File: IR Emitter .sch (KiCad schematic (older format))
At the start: 19 parts

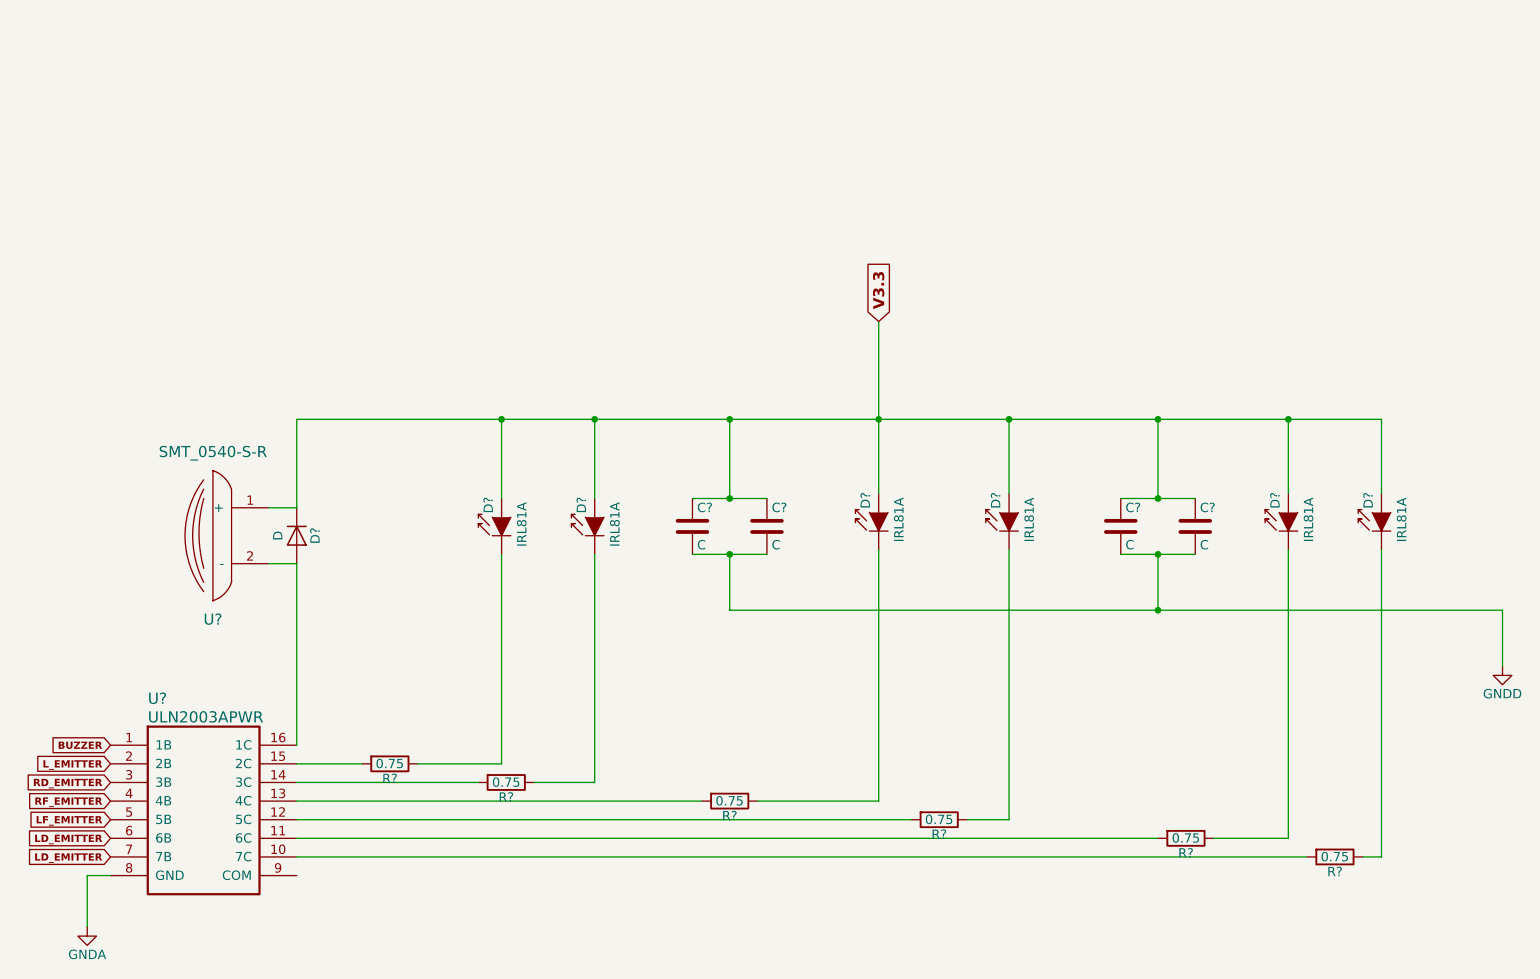
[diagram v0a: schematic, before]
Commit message: created footprint for linear requlator
added footprint for microcontroller linear requlator
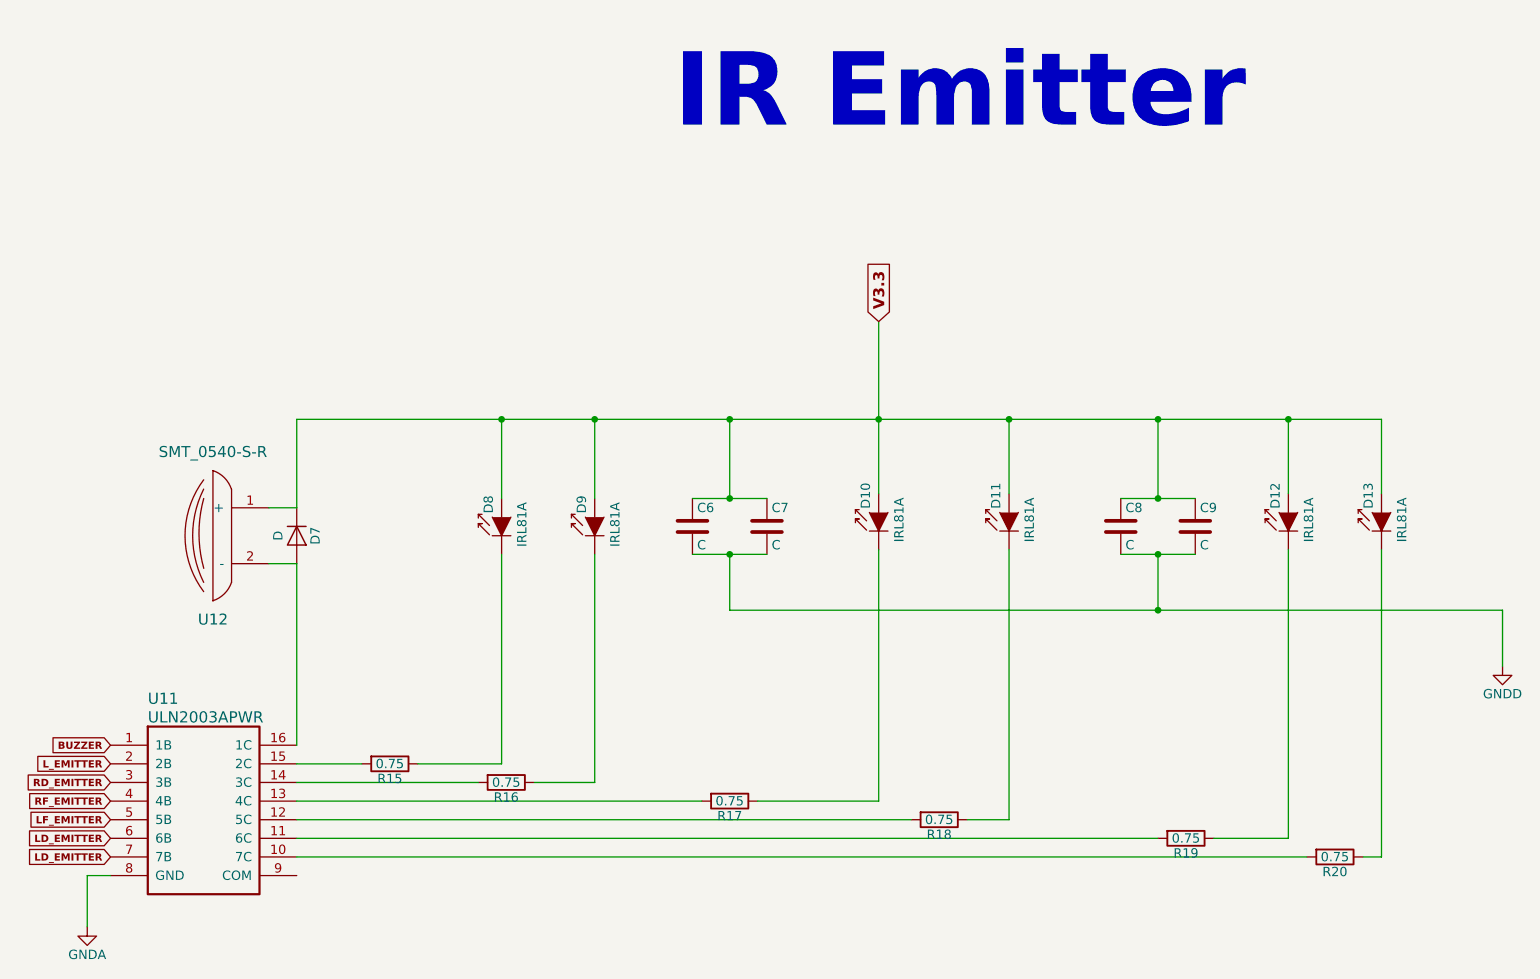
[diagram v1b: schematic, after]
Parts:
- C6, C7, C8, C9: renamed from C?; footprint (none) -> Capacitors_SMD:C_0603
- D10, D11, D12, D13, D8, D9: renamed from D?; footprint LEDs:LED_SideEmitter_Rectangular_W4.5mm_H1.6mm -> LEDs:LED_D5.0mm_Horizontal_O3.81mm_Z3.0mm
- D7: renamed from D?; footprint (none) -> Diodes_SMD:D_0603
- R15, R16, R17, R18, R19, R20: renamed from R?; footprint (none) -> Resistors_SMD:R_0603
- U11: renamed from U?; footprint (none) -> sop:TSSOP16
- U12: renamed from U?; footprint (none) -> micromouse:Buzzer_SMT-0540-S-R
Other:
- note added: "IR Emitter"
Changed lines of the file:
@@
 $EndDescr
 $Comp
-L IRL81A D?
+L IRL81A D9
 U 1 1 59460522
 P 3475 3450
-F 0 "D?" H 3495 3520 50  0000 L CNN
+F 0 "D9" H 3495 3520 50  0000 L CNN
 F 1 "IRL81A" H 3435 3340 50  0000 C CNN
-F 2 "LEDs:LED_SideEmitter_Rectangular_W4.5mm_H1.6mm" H 3475 3625 50  0001 C CNN
+F 2 "LEDs:LED_D5.0mm_Horizontal_O3.81mm_Z3.0mm" H 3475 3625 50  0001 C CNN
 F 3 "" H 3425 3450 50  0000 C CNN
 	1    3475 3450
@@
 $EndComp
 $Comp
-L IRL81A D?
+L IRL81A D10
 U 1 1 59460598
 P 5000 3425
-F 0 "D?" H 5020 3495 50  0000 L CNN
+F 0 "D10" H 5020 3495 50  0000 L CNN
 F 1 "IRL81A" H 4960 3315 50  0000 C CNN
-F 2 "LEDs:LED_SideEmitter_Rectangular_W4.5mm_H1.6mm" H 5000 3600 50  0001 C CNN
+F 2 "LEDs:LED_D5.0mm_Horizontal_O3.81mm_Z3.0mm" H 5000 3600 50  0001 C CNN
 F 3 "" H 4950 3425 50  0000 C CNN
 	1    5000 3425
@@
 $EndComp
 $Comp
-L IRL81A D?
+L IRL81A D11
 U 1 1 5946062F
 P 5700 3425
-F 0 "D?" H 5720 3495 50  0000 L CNN
+F 0 "D11" H 5720 3495 50  0000 L CNN
 F 1 "IRL81A" H 5660 3315 50  0000 C CNN
-F 2 "LEDs:LED_SideEmitter_Rectangular_W4.5mm_H1.6mm" H 5700 3600 50  0001 C CNN
+F 2 "LEDs:LED_D5.0mm_Horizontal_O3.81mm_Z3.0mm" H 5700 3600 50  0001 C CNN
 F 3 "" H 5650 3425 50  0000 C CNN
 	1    5700 3425
@@
 $EndComp
 $Comp
-L IRL81A D?
+L IRL81A D12
 U 1 1 59460667
 P 7200 3425
-F 0 "D?" H 7220 3495 50  0000 L CNN
+F 0 "D12" H 7220 3495 50  0000 L CNN
 F 1 "IRL81A" H 7160 3315 50  0000 C CNN
-F 2 "LEDs:LED_SideEmitter_Rectangular_W4.5mm_H1.6mm" H 7200 3600 50  0001 C CNN
+F 2 "LEDs:LED_D5.0mm_Horizontal_O3.81mm_Z3.0mm" H 7200 3600 50  0001 C CNN
 F 3 "" H 7150 3425 50  0000 C CNN
 	1    7200 3425
@@
 $EndComp
 $Comp
-L R R?
+L R R15
 U 1 1 594607AD
 P 2375 4775
-F 0 "R?" V 2455 4775 50  0000 C CNN
+F 0 "R15" V 2455 4775 50  0000 C CNN
 F 1 "0.75" V 2375 4775 50  0000 C CNN
-F 2 "" V 2305 4775 50  0001 C CNN
+F 2 "Resistors_SMD:R_0603" V 2305 4775 50  0001 C CNN
 F 3 "" H 2375 4775 50  0001 C CNN
 	1    2375 4775
@@
 $EndComp
 $Comp
-L R R?
+L R R16
 U 1 1 59460927
 P 3000 4875
-F 0 "R?" V 3080 4875 50  0000 C CNN
+F 0 "R16" V 3080 4875 50  0000 C CNN
 F 1 "0.75" V 3000 4875 50  0000 C CNN
-F 2 "" V 2930 4875 50  0001 C CNN
+F 2 "Resistors_SMD:R_0603" V 2930 4875 50  0001 C CNN
 F 3 "" H 3000 4875 50  0001 C CNN
 	1    3000 4875
@@
 $EndComp
 $Comp
-L R R?
+L R R17
 U 1 1 59460953
 P 4200 4975
-F 0 "R?" V 4280 4975 50  0000 C CNN
+F 0 "R17" V 4280 4975 50  0000 C CNN
 F 1 "0.75" V 4200 4975 50  0000 C CNN
-F 2 "" V 4130 4975 50  0001 C CNN
+F 2 "Resistors_SMD:R_0603" V 4130 4975 50  0001 C CNN
 F 3 "" H 4200 4975 50  0001 C CNN
 	1    4200 4975
@@
 $EndComp
 $Comp
-L R R?
+L R R18
 U 1 1 5946097C
 P 5325 5075
-F 0 "R?" V 5405 5075 50  0000 C CNN
+F 0 "R18" V 5405 5075 50  0000 C CNN
 F 1 "0.75" V 5325 5075 50  0000 C CNN
-F 2 "" V 5255 5075 50  0001 C CNN
+F 2 "Resistors_SMD:R_0603" V 5255 5075 50  0001 C CNN
 F 3 "" H 5325 5075 50  0001 C CNN
 	1    5325 5075
@@
 $EndComp
 $Comp
-L R R?
+L R R19
 U 1 1 594609A7
 P 6650 5175
-F 0 "R?" V 6730 5175 50  0000 C CNN
+F 0 "R19" V 6730 5175 50  0000 C CNN
 F 1 "0.75" V 6650 5175 50  0000 C CNN
-F 2 "" V 6580 5175 50  0001 C CNN
+F 2 "Resistors_SMD:R_0603" V 6580 5175 50  0001 C CNN
 F 3 "" H 6650 5175 50  0001 C CNN
 	1    6650 5175
@@
 $EndComp
 $Comp
-L R R?
+L R R20
 U 1 1 594609E9
 P 7450 5275
-F 0 "R?" V 7530 5275 50  0000 C CNN
+F 0 "R20" V 7530 5275 50  0000 C CNN
 F 1 "0.75" V 7450 5275 50  0000 C CNN
-F 2 "" V 7380 5275 50  0001 C CNN
+F 2 "Resistors_SMD:R_0603" V 7380 5275 50  0001 C CNN
 F 3 "" H 7450 5275 50  0001 C CNN
 	1    7450 5275
@@
 $EndComp
 $Comp
-L IRL81A D?
+L IRL81A D8
 U 1 1 59460A6B
 P 2975 3450
-F 0 "D?" H 2995 3520 50  0000 L CNN
+F 0 "D8" H 2995 3520 50  0000 L CNN
 F 1 "IRL81A" H 2935 3340 50  0000 C CNN
-F 2 "LEDs:LED_SideEmitter_Rectangular_W4.5mm_H1.6mm" H 2975 3625 50  0001 C CNN
+F 2 "LEDs:LED_D5.0mm_Horizontal_O3.81mm_Z3.0mm" H 2975 3625 50  0001 C CNN
 F 3 "" H 2925 3450 50  0000 C CNN
 	1    2975 3450
@@
 $EndComp
 $Comp
-L IRL81A D?
+L IRL81A D13
 U 1 1 59460AA4
 P 7700 3425
-F 0 "D?" H 7720 3495 50  0000 L CNN
+F 0 "D13" H 7720 3495 50  0000 L CNN
 F 1 "IRL81A" H 7660 3315 50  0000 C CNN
-F 2 "LEDs:LED_SideEmitter_Rectangular_W4.5mm_H1.6mm" H 7700 3600 50  0001 C CNN
+F 2 "LEDs:LED_D5.0mm_Horizontal_O3.81mm_Z3.0mm" H 7700 3600 50  0001 C CNN
 F 3 "" H 7650 3425 50  0000 C CNN
 	1    7700 3425
@@
 $EndComp
 $Comp
-L C C?
+L C C8
 U 1 1 59460ADE
 P 6300 3500
-F 0 "C?" H 6325 3600 50  0000 L CNN
+F 0 "C8" H 6325 3600 50  0000 L CNN
 F 1 "C" H 6325 3400 50  0000 L CNN
-F 2 "" H 6338 3350 50  0001 C CNN
+F 2 "Capacitors_SMD:C_0603" H 6338 3350 50  0001 C CNN
 F 3 "" H 6300 3500 50  0001 C CNN
 	1    6300 3500
@@
 $EndComp
 $Comp
-L C C?
+L C C9
 U 1 1 59460B48
 P 6700 3500
-F 0 "C?" H 6725 3600 50  0000 L CNN
+F 0 "C9" H 6725 3600 50  0000 L CNN
 F 1 "C" H 6725 3400 50  0000 L CNN
-F 2 "" H 6738 3350 50  0001 C CNN
+F 2 "Capacitors_SMD:C_0603" H 6738 3350 50  0001 C CNN
 F 3 "" H 6700 3500 50  0001 C CNN
 	1    6700 3500
@@
 $EndComp
 $Comp
-L C C?
+L C C6
 U 1 1 59460FD6
 P 4000 3500
-F 0 "C?" H 4025 3600 50  0000 L CNN
+F 0 "C6" H 4025 3600 50  0000 L CNN
 F 1 "C" H 4025 3400 50  0000 L CNN
-F 2 "" H 4038 3350 50  0001 C CNN
+F 2 "Capacitors_SMD:C_0603" H 4038 3350 50  0001 C CNN
 F 3 "" H 4000 3500 50  0001 C CNN
 	1    4000 3500
@@
 $EndComp
 $Comp
-L C C?
+L C C7
 U 1 1 59460FDC
 P 4400 3500
-F 0 "C?" H 4425 3600 50  0000 L CNN
+F 0 "C7" H 4425 3600 50  0000 L CNN
 F 1 "C" H 4425 3400 50  0000 L CNN
-F 2 "" H 4438 3350 50  0001 C CNN
+F 2 "Capacitors_SMD:C_0603" H 4438 3350 50  0001 C CNN
 F 3 "" H 4400 3500 50  0001 C CNN
 	1    4400 3500
@@
 	7700 5275 7600 5275
 $Comp
-L ULN2003APWR U?
+L ULN2003APWR U11
 U 1 1 59461B93
 P 875 4675
-F 0 "U?" H 1075 4925 60  0000 L CNN
+F 0 "U11" H 1075 4925 60  0000 L CNN
 F 1 "ULN2003APWR" H 1075 4825 60  0000 L CNN
-F 2 "" H 875 4675 60  0001 C CNN
+F 2 "sop:TSSOP16" H 875 4675 60  0001 C CNN
 F 3 "" H 875 4675 60  0001 C CNN
 	1    875  4675
@@
 $EndComp
 $Comp
-L SMT_0540-S-R U?
+L SMT_0540-S-R U12
 U 1 1 59461CC9
 P 1425 3600
-F 0 "U?" H 1425 3200 59  0000 C CNN
+F 0 "U12" H 1425 3200 59  0000 C CNN
 F 1 "SMT_0540-S-R" H 1425 4100 59  0000 C CNN
-F 2 "" H 1425 3600 59  0001 C CNN
+F 2 "micromouse:Buzzer_SMT-0540-S-R" H 1425 3600 59  0001 C CNN
 F 3 "" H 1425 3600 59  0001 C CNN
 	1    1425 3600
@@
 	1875 3700 1875 4675
 $Comp
-L GNDD #PWR?
+L GNDD #PWR08
 U 1 1 5946214E
 P 8350 4250
-F 0 "#PWR?" H 8350 4000 50  0001 C CNN
+F 0 "#PWR08" H 8350 4000 50  0001 C CNN
 F 1 "GNDD" H 8350 4100 50  0000 C CNN
 F 2 "" H 8350 4250 50  0001 C CNN
@@
 Connection ~ 2975 2925
 $Comp
-L D D?
+L D D7
 U 1 1 5946296D
 P 1875 3550
-F 0 "D?" H 1875 3650 50  0000 C CNN
+F 0 "D7" H 1875 3650 50  0000 C CNN
 F 1 "D" H 1875 3450 50  0000 C CNN
-F 2 "" H 1875 3550 50  0001 C CNN
+F 2 "Diodes_SMD:D_0603" H 1875 3550 50  0001 C CNN
 F 3 "" H 1875 3550 50  0001 C CNN
 	1    1875 3550
@@
 LD_EMITTER
 $Comp
-L GNDA #PWR?
+L GNDA #PWR09
 U 1 1 59463543
 P 750 5650
-F 0 "#PWR?" H 750 5400 50  0001 C CNN
+F 0 "#PWR09" H 750 5400 50  0001 C CNN
 F 1 "GNDA" H 750 5500 50  0000 C CNN
 F 2 "" H 750 5650 50  0001 C CNN
@@
 Wire Wire Line
 	750  5375 875  5375
+Text Notes 3900 1400 0    394  ~ 79
+IR Emitter
 $EndSCHEMATC
